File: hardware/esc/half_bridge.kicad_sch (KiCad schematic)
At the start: 4 parts, among them Q1 MCG4D8N04YHE3-TP, Q2 MCG4D8N04YHE3-TP

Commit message: h/feat: preliminary rev 2 schematic
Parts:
- Q1, Q2: value MCG4D8N04YHE3-TP -> NVTFWS003N04XMTAG
- renumbered R21 to R16, R22 to R17
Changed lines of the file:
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@@
 			)
 		)
-		(property "Value" "MCG4D8N04YHE3-TP"
+		(property "Value" "NVTFWS003N04XMTAG"
 			(at 148.59 119.3799 0)
 			(show_name no)
@@
 			)
 		)
-		(property "Datasheet" "https://www.mccsemi.com/pdf/Products/MCGL2D1N03YL(PDFN3333-B).pdf"
+		(property "Datasheet" "https://www.onsemi.jp/download/data-sheet/pdf/nvtfws003n04xm-d.pdf"
 			(at 148.59 307.95 0)
 			(hide yes)
@@
 		(dnp no)
 		(fields_autoplaced yes)
-		(property "Reference" "R22"
+		(property "Reference" "R17"
 			(at 121.92 113.03 90)
 			(show_name no)
@@
 			(project "esc"
 				(path "/297cf99d-9b04-43d6-b8b3-ae230a9c184d/0070120e-1e03-4d14-907f-a744278e5b35/630a3906-3064-4c40-b1fe-9d962eb3859e"
-					(reference "R22")
+					(reference "R17")
 					(unit 1)
 				)
 				(path "/297cf99d-9b04-43d6-b8b3-ae230a9c184d/0070120e-1e03-4d14-907f-a744278e5b35/7dce918c-6576-40aa-9b22-b13330cd5c9a"
-					(reference "R26")
+					(reference "R21")
 					(unit 1)
 				)
 				(path "/297cf99d-9b04-43d6-b8b3-ae230a9c184d/0070120e-1e03-4d14-907f-a744278e5b35/cc02f46e-3047-4d54-8b43-7b4556e32b77"
-					(reference "R24")
+					(reference "R19")
 					(unit 1)
 				)
 				(path "/297cf99d-9b04-43d6-b8b3-ae230a9c184d/03a49181-e11c-4f7c-b77f-c7fb3a5b342f/630a3906-3064-4c40-b1fe-9d962eb3859e"
+					(reference "R55")
+					(unit 1)
+				)
+				(path "/297cf99d-9b04-43d6-b8b3-ae230a9c184d/03a49181-e11c-4f7c-b77f-c7fb3a5b342f/7dce918c-6576-40aa-9b22-b13330cd5c9a"
+					(reference "R53")
+					(unit 1)
+				)
+				(path "/297cf99d-9b04-43d6-b8b3-ae230a9c184d/03a49181-e11c-4f7c-b77f-c7fb3a5b342f/cc02f46e-3047-4d54-8b43-7b4556e32b77"
+					(reference "R51")
+					(unit 1)
+				)
+				(path "/297cf99d-9b04-43d6-b8b3-ae230a9c184d/7efa9175-24bd-43e0-8b42-d74300bece59/630a3906-3064-4c40-b1fe-9d962eb3859e"
+					(reference "R72")
+					(unit 1)
+				)
+				(path "/297cf99d-9b04-43d6-b8b3-ae230a9c184d/7efa9175-24bd-43e0-8b42-d74300bece59/7dce918c-6576-40aa-9b22-b13330cd5c9a"
+					(reference "R70")
+					(unit 1)
+				)
+				(path "/297cf99d-9b04-43d6-b8b3-ae230a9c184d/7efa9175-24bd-43e0-8b42-d74300bece59/cc02f46e-3047-4d54-8b43-7b4556e32b77"
 					(reference "R68")
 					(unit 1)
 				)
-				(path "/297cf99d-9b04-43d6-b8b3-ae230a9c184d/03a49181-e11c-4f7c-b77f-c7fb3a5b342f/7dce918c-6576-40aa-9b22-b13330cd5c9a"
-					(reference "R66")
-					(unit 1)
-				)
-				(path "/297cf99d-9b04-43d6-b8b3-ae230a9c184d/03a49181-e11c-4f7c-b77f-c7fb3a5b342f/cc02f46e-3047-4d54-8b43-7b4556e32b77"
-					(reference "R64")
-					(unit 1)
-				)
-				(path "/297cf99d-9b04-43d6-b8b3-ae230a9c184d/7efa9175-24bd-43e0-8b42-d74300bece59/630a3906-3064-4c40-b1fe-9d962eb3859e"
-					(reference "R89")
-					(unit 1)
-				)
-				(path "/297cf99d-9b04-43d6-b8b3-ae230a9c184d/7efa9175-24bd-43e0-8b42-d74300bece59/7dce918c-6576-40aa-9b22-b13330cd5c9a"
-					(reference "R87")
-					(unit 1)
-				)
-				(path "/297cf99d-9b04-43d6-b8b3-ae230a9c184d/7efa9175-24bd-43e0-8b42-d74300bece59/cc02f46e-3047-4d54-8b43-7b4556e32b77"
-					(reference "R85")
-					(unit 1)
-				)
 				(path "/297cf99d-9b04-43d6-b8b3-ae230a9c184d/ed8f9e9f-3338-4398-856c-63cd3b359b47/630a3906-3064-4c40-b1fe-9d962eb3859e"
-					(reference "R47")
+					(reference "R38")
 					(unit 1)
 				)
 				(path "/297cf99d-9b04-43d6-b8b3-ae230a9c184d/ed8f9e9f-3338-4398-856c-63cd3b359b47/7dce918c-6576-40aa-9b22-b13330cd5c9a"
-					(reference "R45")
+					(reference "R36")
 					(unit 1)
 				)
 				(path "/297cf99d-9b04-43d6-b8b3-ae230a9c184d/ed8f9e9f-3338-4398-856c-63cd3b359b47/cc02f46e-3047-4d54-8b43-7b4556e32b77"
-					(reference "R43")
+					(reference "R34")
 					(unit 1)
 				)
@@
 		(dnp no)
 		(fields_autoplaced yes)
-		(property "Reference" "R21"
+		(property "Reference" "R16"
 			(at 121.92 77.47 90)
 			(show_name no)
@@
 			(project "esc"
 				(path "/297cf99d-9b04-43d6-b8b3-ae230a9c184d/0070120e-1e03-4d14-907f-a744278e5b35/630a3906-3064-4c40-b1fe-9d962eb3859e"
-					(reference "R21")
+					(reference "R16")
 					(unit 1)
 				)
 				(path "/297cf99d-9b04-43d6-b8b3-ae230a9c184d/0070120e-1e03-4d14-907f-a744278e5b35/7dce918c-6576-40aa-9b22-b13330cd5c9a"
-					(reference "R25")
+					(reference "R20")
 					(unit 1)
 				)
 				(path "/297cf99d-9b04-43d6-b8b3-ae230a9c184d/0070120e-1e03-4d14-907f-a744278e5b35/cc02f46e-3047-4d54-8b43-7b4556e32b77"
-					(reference "R23")
+					(reference "R18")
 					(unit 1)
 				)
 				(path "/297cf99d-9b04-43d6-b8b3-ae230a9c184d/03a49181-e11c-4f7c-b77f-c7fb3a5b342f/630a3906-3064-4c40-b1fe-9d962eb3859e"
+					(reference "R54")
+					(unit 1)
+				)
+				(path "/297cf99d-9b04-43d6-b8b3-ae230a9c184d/03a49181-e11c-4f7c-b77f-c7fb3a5b342f/7dce918c-6576-40aa-9b22-b13330cd5c9a"
+					(reference "R52")
+					(unit 1)
+				)
+				(path "/297cf99d-9b04-43d6-b8b3-ae230a9c184d/03a49181-e11c-4f7c-b77f-c7fb3a5b342f/cc02f46e-3047-4d54-8b43-7b4556e32b77"
+					(reference "R50")
+					(unit 1)
+				)
+				(path "/297cf99d-9b04-43d6-b8b3-ae230a9c184d/7efa9175-24bd-43e0-8b42-d74300bece59/630a3906-3064-4c40-b1fe-9d962eb3859e"
+					(reference "R71")
+					(unit 1)
+				)
+				(path "/297cf99d-9b04-43d6-b8b3-ae230a9c184d/7efa9175-24bd-43e0-8b42-d74300bece59/7dce918c-6576-40aa-9b22-b13330cd5c9a"
+					(reference "R69")
+					(unit 1)
+				)
+				(path "/297cf99d-9b04-43d6-b8b3-ae230a9c184d/7efa9175-24bd-43e0-8b42-d74300bece59/cc02f46e-3047-4d54-8b43-7b4556e32b77"
 					(reference "R67")
 					(unit 1)
 				)
-				(path "/297cf99d-9b04-43d6-b8b3-ae230a9c184d/03a49181-e11c-4f7c-b77f-c7fb3a5b342f/7dce918c-6576-40aa-9b22-b13330cd5c9a"
-					(reference "R65")
-					(unit 1)
-				)
-				(path "/297cf99d-9b04-43d6-b8b3-ae230a9c184d/03a49181-e11c-4f7c-b77f-c7fb3a5b342f/cc02f46e-3047-4d54-8b43-7b4556e32b77"
-					(reference "R63")
-					(unit 1)
-				)
-				(path "/297cf99d-9b04-43d6-b8b3-ae230a9c184d/7efa9175-24bd-43e0-8b42-d74300bece59/630a3906-3064-4c40-b1fe-9d962eb3859e"
-					(reference "R88")
-					(unit 1)
-				)
-				(path "/297cf99d-9b04-43d6-b8b3-ae230a9c184d/7efa9175-24bd-43e0-8b42-d74300bece59/7dce918c-6576-40aa-9b22-b13330cd5c9a"
-					(reference "R86")
-					(unit 1)
-				)
-				(path "/297cf99d-9b04-43d6-b8b3-ae230a9c184d/7efa9175-24bd-43e0-8b42-d74300bece59/cc02f46e-3047-4d54-8b43-7b4556e32b77"
-					(reference "R84")
-					(unit 1)
-				)
 				(path "/297cf99d-9b04-43d6-b8b3-ae230a9c184d/ed8f9e9f-3338-4398-856c-63cd3b359b47/630a3906-3064-4c40-b1fe-9d962eb3859e"
-					(reference "R46")
+					(reference "R37")
 					(unit 1)
 				)
 				(path "/297cf99d-9b04-43d6-b8b3-ae230a9c184d/ed8f9e9f-3338-4398-856c-63cd3b359b47/7dce918c-6576-40aa-9b22-b13330cd5c9a"
-					(reference "R44")
+					(reference "R35")
 					(unit 1)
 				)
 				(path "/297cf99d-9b04-43d6-b8b3-ae230a9c184d/ed8f9e9f-3338-4398-856c-63cd3b359b47/cc02f46e-3047-4d54-8b43-7b4556e32b77"
-					(reference "R42")
+					(reference "R33")
 					(unit 1)
 				)
@@
 			)
 		)
-		(property "Value" "MCG4D8N04YHE3-TP"
+		(property "Value" "NVTFWS003N04XMTAG"
 			(at 148.59 83.8199 0)
 			(show_name no)
@@
 			)
 		)
-		(property "Datasheet" "https://www.mccsemi.com/pdf/Products/MCGL2D1N03YL(PDFN3333-B).pdf"
+		(property "Datasheet" "https://www.onsemi.jp/download/data-sheet/pdf/nvtfws003n04xm-d.pdf"
 			(at 148.59 272.39 0)
 			(hide yes)

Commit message: chore: prep: footprints, 3d models, pcb
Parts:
- Q1, Q2: footprint Stratus:MCG4D8N04YHE3-TP -> Stratus:NVTFWS003N04XMTAG
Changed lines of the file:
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@@
 			)
 		)
-		(property "Footprint" "Stratus:MCG4D8N04YHE3-TP"
+		(property "Footprint" "Stratus:NVTFWS003N04XMTAG"
 			(at 148.59 207.95 0)
 			(hide yes)
@@
 			)
 		)
-		(property "Footprint" "Stratus:MCG4D8N04YHE3-TP"
+		(property "Footprint" "Stratus:NVTFWS003N04XMTAG"
 			(at 148.59 172.39 0)
 			(hide yes)

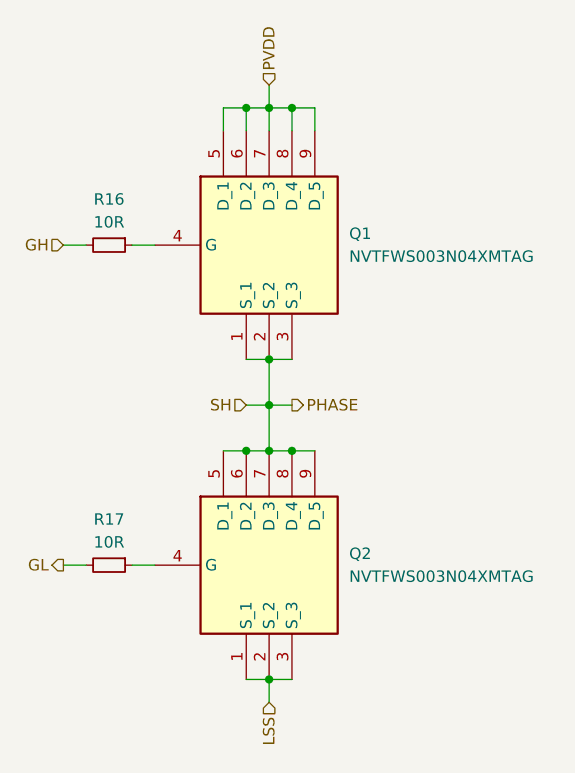
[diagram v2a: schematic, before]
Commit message: h/feat: gate drive routing + prelim layout
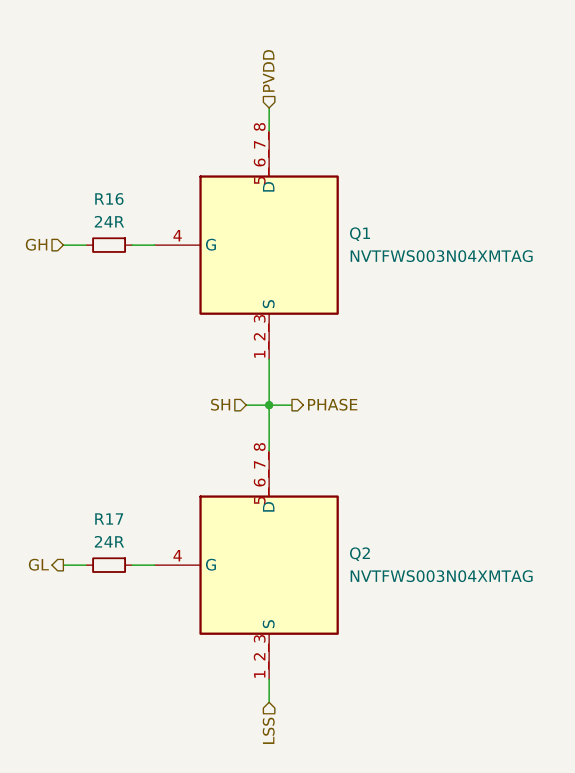
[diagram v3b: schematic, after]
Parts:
- R16, R17: value 10R -> 24R; footprint Resistor_SMD:R_0402_1005Metric -> Stratus:R_0402
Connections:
- net LSS: now also Q2.1_2_3 (S); no longer Q2.1 (S_1), Q2.2 (S_2), Q2.3 (S_3)
- net PHASE: now also Q1.1_2_3 (S), Q2.5_6_7_8 (D); no longer Q1.1 (S_1), Q1.2 (S_2), Q1.3 (S_3), Q2.5 (D_1), Q2.6 (D_2), Q2.7 (D_3), Q2.8 (D_4), Q2.9 (D_5)
- net PVDD: now also Q1.5_6_7_8 (D); no longer Q1.5 (D_1), Q1.6 (D_2), Q1.7 (D_3), Q1.8 (D_4), Q1.9 (D_5)
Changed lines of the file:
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@@
-	)
-	(junction
-		(at 137.16 105.41)
-		(diameter 0)
-		(color 0 0 0 0)
-	)
-	(junction
-		(at 142.24 67.31)
-		(diameter 0)
-		(color 0 0 0 0)
-	)
-	(junction
-		(at 139.7 105.41)
-		(diameter 0)
-		(color 0 0 0 0)
-	)
-	(junction
-		(at 137.16 67.31)
-		(diameter 0)
-		(color 0 0 0 0)
 	)
 	(junction
@@
 		(color 0 0 0 0)
 	)
-	(junction
-		(at 142.24 105.41)
-		(diameter 0)
-		(color 0 0 0 0)
-	)
-	(junction
-		(at 139.7 130.81)
-		(diameter 0)
-		(color 0 0 0 0)
-	)
-	(junction
-		(at 139.7 95.25)
-		(diameter 0)
-		(color 0 0 0 0)
-	)
-	(junction
-		(at 139.7 67.31)
-		(diameter 0)
-		(color 0 0 0 0)
-	)
-	(wire
-		(pts
-			(xy 139.7 64.77) (xy 139.7 67.31)
-		)
-		(stroke
-			(width 0)
-			(type default)
-		)
-	)
-	(wire
-		(pts
-			(xy 137.16 130.81) (xy 139.7 130.81)
-		)
-		(stroke
-			(width 0)
-			(type default)
-		)
-	)
-	(wire
-		(pts
-			(xy 139.7 105.41) (xy 142.24 105.41)
-		)
-		(stroke
-			(width 0)
-			(type default)
-		)
-	)
 	(wire
 		(pts
@@
 	(wire
 		(pts
-			(xy 137.16 67.31) (xy 139.7 67.31)
-		)
-		(stroke
-			(width 0)
-			(type default)
-		)
-	)
-	(wire
-		(pts
-			(xy 139.7 95.25) (xy 142.24 95.25)
-		)
-		(stroke
-			(width 0)
-			(type default)
-		)
-	)
-	(wire
-		(pts
 			(xy 139.7 95.25) (xy 139.7 100.33)
 		)
@@
 	(wire
 		(pts
-			(xy 134.62 67.31) (xy 137.16 67.31)
-		)
-		(stroke
-			(width 0)
-			(type default)
-		)
-	)
-	(wire
-		(pts
-			(xy 142.24 105.41) (xy 144.78 105.41)
-		)
-		(stroke
-			(width 0)
-			(type default)
-		)
-	)
-	(wire
-		(pts
 			(xy 139.7 133.35) (xy 139.7 130.81)
 		)
@@
 	(wire
 		(pts
-			(xy 137.16 95.25) (xy 139.7 95.25)
-		)
-		(stroke
-			(width 0)
-			(type default)
-		)
-	)
-	(wire
-		(pts
 			(xy 116.84 118.11) (xy 119.38 118.11)
 		)
@@
 	(wire
 		(pts
-			(xy 137.16 67.31) (xy 137.16 69.85)
-		)
-		(stroke
-			(width 0)
-			(type default)
-		)
-	)
-	(wire
-		(pts
-			(xy 142.24 67.31) (xy 142.24 69.85)
-		)
-		(stroke
-			(width 0)
-			(type default)
-		)
-	)
-	(wire
-		(pts
-			(xy 144.78 67.31) (xy 144.78 69.85)
-		)
-		(stroke
-			(width 0)
-			(type default)
-		)
-	)
-	(wire
-		(pts
 			(xy 139.7 67.31) (xy 139.7 69.85)
 		)
@@
 	(wire
 		(pts
-			(xy 139.7 130.81) (xy 142.24 130.81)
-		)
-		(stroke
-			(width 0)
-			(type default)
-		)
-	)
-	(wire
-		(pts
 			(xy 137.16 100.33) (xy 139.7 100.33)
 		)
@@
 		(pts
 			(xy 116.84 82.55) (xy 119.38 82.55)
-		)
-		(stroke
-			(width 0)
-			(type default)
-		)
-	)
-	(wire
-		(pts
-			(xy 134.62 105.41) (xy 137.16 105.41)
-		)
-		(stroke
-			(width 0)
-			(type default)
-		)
-	)
-	(wire
-		(pts
-			(xy 134.62 69.85) (xy 134.62 67.31)
-		)
-		(stroke
-			(width 0)
-			(type default)
-		)
-	)
-	(wire
-		(pts
-			(xy 142.24 67.31) (xy 144.78 67.31)
-		)
-		(stroke
-			(width 0)
-			(type default)
-		)
-	)
-	(wire
-		(pts
-			(xy 137.16 105.41) (xy 139.7 105.41)
-		)
-		(stroke
-			(width 0)
-			(type default)
-		)
-	)
-	(wire
-		(pts
-			(xy 139.7 67.31) (xy 142.24 67.31)
 		)
 		(stroke
@@
 	(hierarchical_label "PVDD"
 		(shape input)
-		(at 139.7 64.77 90)
+		(at 139.7 67.31 90)
 		(effects
 			(font
@@
 			)
 		)
-		(pin "2"
-		)
-		(pin "9"
-		)
-		(pin "6"
-		)
-		(pin "7"
-		)
-		(pin "8"
+		(pin "5_6_7_8"
 		)
 		(pin "4"
 		)
-		(pin "1"
-		)
-		(pin "3"
-		)
-		(pin "5"
+		(pin "1_2_3"
 		)
 		(instances
@@
 			)
 		)
-		(property "Value" "10R"
+		(property "Value" "24R"
 			(at 121.92 115.57 90)
 			(show_name no)
@@
 			)
 		)
-		(property "Footprint" "Resistor_SMD:R_0402_1005Metric"
+		(property "Footprint" "Stratus:R_0402"
 			(at 121.92 118.11 0)
 			(hide yes)
@@
 			)
 		)
-		(property "Value" "10R"
+		(property "Value" "24R"
 			(at 121.92 80.01 90)
 			(show_name no)
@@
 			)
 		)
-		(property "Footprint" "Resistor_SMD:R_0402_1005Metric"
+		(property "Footprint" "Stratus:R_0402"
 			(at 121.92 82.55 0)
 			(hide yes)
@@
 	)
 	(symbol
-		(lib_name "MCGL2D1N03YL-TP_2")
+		(lib_name "MCGL2D1N03YL-TP_1")
 		(lib_id "MCGL2D1N03YL-TP:MCGL2D1N03YL-TP")
 		(at 127 77.47 0)
@@
 			)
 		)
-		(pin "2"
-		)
-		(pin "9"
-		)
-		(pin "6"
-		)
-		(pin "7"
-		)
-		(pin "8"
+		(pin "1_2_3"
+		)
+		(pin "5_6_7_8"
 		)
 		(pin "4"
 		)
-		(pin "1"
-		)
-		(pin "3"
-		)
-		(pin "5"
-		)
 		(instances

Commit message: h/feat: placement; power stage pending
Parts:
- R16, R17: value 24R -> 27R
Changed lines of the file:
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@@
 			)
 		)
-		(property "Value" "24R"
+		(property "Value" "27R"
 			(at 121.92 115.57 90)
 			(show_name no)
@@
 			)
 		)
-		(property "Value" "24R"
+		(property "Value" "27R"
 			(at 121.92 80.01 90)
 			(show_name no)

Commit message: h/feat: rework power stage: power drv8300 from 10v; remove 5v FC passthrough
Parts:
- Q1, Q2: footprint Stratus:NVTFWS003N04XMTAG -> Stratus:CSD17575Q3
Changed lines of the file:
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@@
 			)
 		)
-		(property "Footprint" "Stratus:NVTFWS003N04XMTAG"
+		(property "Footprint" "Stratus:CSD17575Q3"
 			(at 148.59 207.95 0)
 			(hide yes)
@@
 			)
 		)
-		(property "Footprint" "Stratus:NVTFWS003N04XMTAG"
+		(property "Footprint" "Stratus:CSD17575Q3"
 			(at 148.59 172.39 0)
 			(hide yes)

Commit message: h/fix: update FET name in schematic
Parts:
- Q1, Q2: value NVTFWS003N04XMTAG -> CSD17575Q3
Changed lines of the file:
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@@
 			)
 		)
-		(property "Value" "NVTFWS003N04XMTAG"
+		(property "Value" "CSD17575Q3"
 			(at 148.59 119.3799 0)
 			(show_name no)
@@
 			)
 		)
-		(property "Value" "NVTFWS003N04XMTAG"
+		(property "Value" "CSD17575Q3"
 			(at 148.59 83.8199 0)
 			(show_name no)

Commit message: chore: add BOM
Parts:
- Q1, Q2: Height 0.85 -> (none); LCSC# (none) -> C529277; MFR (none) -> TI; MPN (none) -> CSD17575Q3; Manufacturer_Name MCC -> (none); Manufacturer_Part_Number MCG4D8N04YHE3-TP -> (none)
- R16, R17: LCSC# (none) -> C138021; MFR (none) -> Yageo; MPN (none) -> RC0402FR-0727RL; Manufacturer_Name Yageo -> (none); Manufacturer_Part_Number RC0402FR-0710RL -> (none)
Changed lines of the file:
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@@
 			)
 		)
-		(property "Datasheet" "https://www.onsemi.jp/download/data-sheet/pdf/nvtfws003n04xm-d.pdf"
+		(property "Datasheet" "https://www.ti.com/lit/ds/symlink/csd17575q3.pdf"
 			(at 148.59 307.95 0)
 			(hide yes)
@@
 			)
 		)
-		(property "Description" "N-Channel MOSFET"
+		(property "Description" "N-Channel MOSFET 30V 60A 2.8W"
 			(at 127 113.03 0)
 			(hide yes)
@@
 			)
 		)
-		(property "Height" "0.85"
-			(at 148.59 507.95 0)
-			(hide yes)
-			(show_name no)
-			(do_not_autoplace no)
-			(effects
-				(font
-					(size 1.27 1.27)
-				)
-				(justify left top)
-			)
-		)
-		(property "Manufacturer_Name" "MCC"
-			(at 148.59 607.95 0)
-			(hide yes)
-			(show_name no)
-			(do_not_autoplace no)
-			(effects
-				(font
-					(size 1.27 1.27)
-				)
-				(justify left top)
-			)
-		)
-		(property "Manufacturer_Part_Number" "MCG4D8N04YHE3-TP"
-			(at 148.59 707.95 0)
-			(hide yes)
-			(show_name no)
-			(do_not_autoplace no)
-			(effects
-				(font
-					(size 1.27 1.27)
-				)
-				(justify left top)
-			)
-		)
-		(property "Mouser Part Number" ""
-			(at 148.59 807.95 0)
-			(hide yes)
-			(show_name no)
-			(do_not_autoplace no)
-			(effects
-				(font
-					(size 1.27 1.27)
-				)
-				(justify left top)
-			)
-		)
-		(property "Mouser Price/Stock" ""
-			(at 148.59 907.95 0)
-			(hide yes)
-			(show_name no)
-			(do_not_autoplace no)
-			(effects
-				(font
-					(size 1.27 1.27)
-				)
-				(justify left top)
-			)
-		)
-		(property "Arrow Part Number" ""
-			(at 148.59 1007.95 0)
-			(hide yes)
-			(show_name no)
-			(do_not_autoplace no)
-			(effects
-				(font
-					(size 1.27 1.27)
-				)
-				(justify left top)
-			)
-		)
-		(property "Arrow Price/Stock" ""
-			(at 148.59 1107.95 0)
-			(hide yes)
-			(show_name no)
-			(do_not_autoplace no)
-			(effects
-				(font
-					(size 1.27 1.27)
-				)
-				(justify left top)
+		(property "LCSC#" "C529277"
+			(at 127 113.03 0)
+			(hide yes)
+			(show_name no)
+			(do_not_autoplace no)
+			(effects
+				(font
+					(size 1.27 1.27)
+				)
+			)
+		)
+		(property "MFR" "TI"
+			(at 127 113.03 0)
+			(hide yes)
+			(show_name no)
+			(do_not_autoplace no)
+			(effects
+				(font
+					(size 1.27 1.27)
+				)
+			)
+		)
+		(property "MPN" "CSD17575Q3"
+			(at 127 113.03 0)
+			(hide yes)
+			(show_name no)
+			(do_not_autoplace no)
+			(effects
+				(font
+					(size 1.27 1.27)
+				)
 			)
 		)
@@
 			)
 		)
-		(property "Description" "Resistor, small symbol"
+		(property "Description" "0402 27R"
 			(at 121.92 118.11 0)
 			(hide yes)
@@
 			)
 		)
-		(property "Manufacturer_Name" "Yageo"
+		(property "LCSC#" "C138021"
 			(at 121.92 118.11 90)
 			(hide yes)
@@
 			)
 		)
-		(property "Manufacturer_Part_Number" "RC0402FR-0710RL"
+		(property "MFR" "Yageo"
+			(at 121.92 118.11 90)
+			(hide yes)
+			(show_name no)
+			(do_not_autoplace no)
+			(effects
+				(font
+					(size 1.27 1.27)
+				)
+			)
+		)
+		(property "MPN" "RC0402FR-0727RL"
 			(at 121.92 118.11 90)
 			(hide yes)
@@
 			)
 		)
-		(property "Description" "Resistor, small symbol"
+		(property "Description" "0402 27R"
 			(at 121.92 82.55 0)
 			(hide yes)
@@
 			)
 		)
-		(property "Manufacturer_Name" "Yageo"
+		(property "LCSC#" "C138021"
 			(at 121.92 82.55 90)
 			(hide yes)
@@
 			)
 		)
-		(property "Manufacturer_Part_Number" "RC0402FR-0710RL"
+		(property "MFR" "Yageo"
+			(at 121.92 82.55 90)
+			(hide yes)
+			(show_name no)
+			(do_not_autoplace no)
+			(effects
+				(font
+					(size 1.27 1.27)
+				)
+			)
+		)
+		(property "MPN" "RC0402FR-0727RL"
 			(at 121.92 82.55 90)
 			(hide yes)
@@
 			)
 		)
-		(property "Datasheet" "https://www.onsemi.jp/download/data-sheet/pdf/nvtfws003n04xm-d.pdf"
+		(property "Datasheet" "https://www.ti.com/lit/ds/symlink/csd17575q3.pdf"
 			(at 148.59 272.39 0)
 			(hide yes)
@@
 			)
 		)
-		(property "Description" "N-Channel MOSFET"
+		(property "Description" "N-Channel MOSFET 30V 60A 2.8W"
 			(at 127 77.47 0)
 			(hide yes)
@@
 			)
 		)
-		(property "Height" "0.85"
-			(at 148.59 472.39 0)
-			(hide yes)
-			(show_name no)
-			(do_not_autoplace no)
-			(effects
-				(font
-					(size 1.27 1.27)
-				)
-				(justify left top)
-			)
-		)
-		(property "Manufacturer_Name" "MCC"
-			(at 148.59 572.39 0)
-			(hide yes)
-			(show_name no)
-			(do_not_autoplace no)
-			(effects
-				(font
-					(size 1.27 1.27)
-				)
-				(justify left top)
-			)
-		)
-		(property "Manufacturer_Part_Number" "MCG4D8N04YHE3-TP"
-			(at 148.59 672.39 0)
-			(hide yes)
-			(show_name no)
-			(do_not_autoplace no)
-			(effects
-				(font
-					(size 1.27 1.27)
-				)
-				(justify left top)
-			)
-		)
-		(property "Mouser Part Number" ""
-			(at 148.59 772.39 0)
-			(hide yes)
-			(show_name no)
-			(do_not_autoplace no)
-			(effects
-				(font
-					(size 1.27 1.27)
-				)
-				(justify left top)
-			)
-		)
-		(property "Mouser Price/Stock" ""
-			(at 148.59 872.39 0)
-			(hide yes)
-			(show_name no)
-			(do_not_autoplace no)
-			(effects
-				(font
-					(size 1.27 1.27)
-				)
-				(justify left top)
-			)
-		)
-		(property "Arrow Part Number" ""
-			(at 148.59 972.39 0)
-			(hide yes)
-			(show_name no)
-			(do_not_autoplace no)
-			(effects
-				(font
-					(size 1.27 1.27)
-				)
-				(justify left top)
-			)
-		)
-		(property "Arrow Price/Stock" ""
-			(at 148.59 1072.39 0)
-			(hide yes)
-			(show_name no)
-			(do_not_autoplace no)
-			(effects
-				(font
-					(size 1.27 1.27)
-				)
-				(justify left top)
-			)
-		)
+		(property "LCSC#" "C529277"
+			(at 127 77.47 0)
+			(hide yes)
+			(show_name no)
+			(do_not_autoplace no)
+			(effects
+				(font
+					(size 1.27 1.27)
+				)
+			)
+		)
+		(property "MFR" "TI"
+			(at 127 77.47 0)
+			(hide yes)
+			(show_name no)
+			(do_not_autoplace no)
+			(effects
+				(font
+					(size 1.27 1.27)
+				)
+			)
+		)
+		(property "MPN" "CSD17575Q3"
+			(at 127 77.47 0)
+			(hide yes)
+			(show_name no)
+			(do_not_autoplace no)
+			(effects
+				(font
+					(size 1.27 1.27)
+				)
+			)
+		)

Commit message: h: prep for rev 3; layout, stackup changes
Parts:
- R16, R17: value 27R -> 10R; LCSC# C138021 -> C138066; MPN RC0402FR-0727RL -> RC0402FR-0710RL
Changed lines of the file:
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@@
 			)
 		)
-		(property "Value" "27R"
+		(property "Value" "10R"
 			(at 121.92 115.57 90)
 			(show_name no)
@@
 			)
 		)
-		(property "Description" "0402 27R"
+		(property "Description" "0402 10R"
 			(at 121.92 118.11 0)
 			(hide yes)
@@
 			)
 		)
-		(property "LCSC#" "C138021"
+		(property "LCSC#" "C138066"
 			(at 121.92 118.11 90)
 			(hide yes)
@@
 			)
 		)
-		(property "MPN" "RC0402FR-0727RL"
+		(property "MPN" "RC0402FR-0710RL"
 			(at 121.92 118.11 90)
 			(hide yes)
@@
 			)
 		)
-		(property "Value" "27R"
+		(property "Value" "10R"
 			(at 121.92 80.01 90)
 			(show_name no)
@@
 			)
 		)
-		(property "Description" "0402 27R"
+		(property "Description" "0402 10R"
 			(at 121.92 82.55 0)
 			(hide yes)
@@
 			)
 		)
-		(property "LCSC#" "C138021"
+		(property "LCSC#" "C138066"
 			(at 121.92 82.55 90)
 			(hide yes)
@@
 			)
 		)
-		(property "MPN" "RC0402FR-0727RL"
+		(property "MPN" "RC0402FR-0710RL"
 			(at 121.92 82.55 90)
 			(hide yes)
